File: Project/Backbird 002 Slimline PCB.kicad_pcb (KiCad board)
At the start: 2 copper layers, 14 x 116 mm, 8 parts

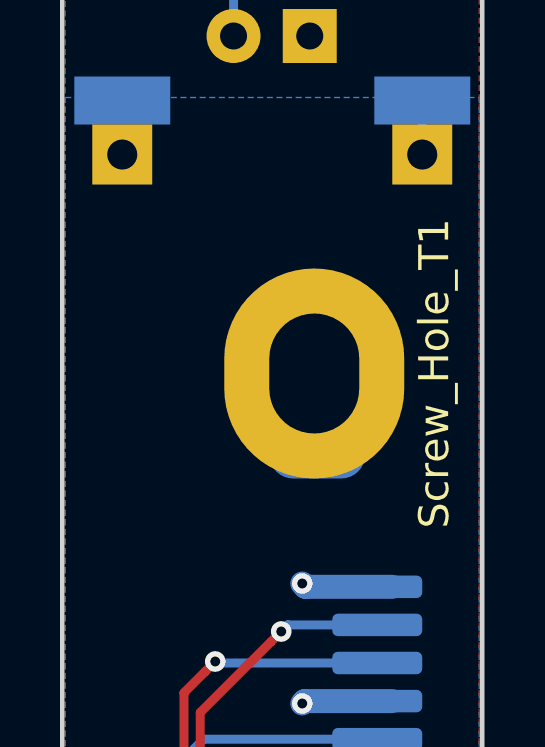
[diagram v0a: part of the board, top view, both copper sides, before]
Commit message: Moved top screw hole closer to edge
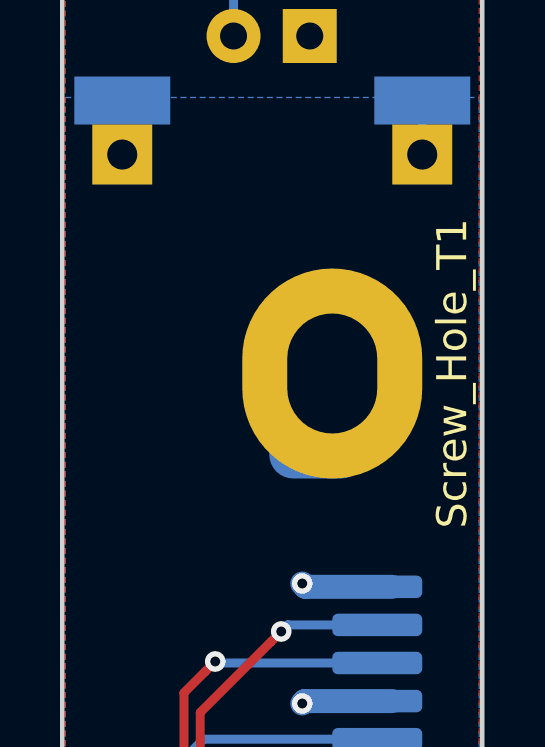
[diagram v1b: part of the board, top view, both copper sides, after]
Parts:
- moved Screw_Hole_T1 0.60 mm to (109.3, 49.5)
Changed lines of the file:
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@@
   )
   (module ProjectFootprints:Blackbird002_Slimline_PCB_Screw_Long (layer F.Cu)
-    (at 108.7 49.48 90)
+    (at 109.3 49.48 90)
     (fp_text reference Screw_Hole_T1 (at 0 4 90) (layer F.SilkS)
       (effects (font (size 1 1) (thickness 0.15)))

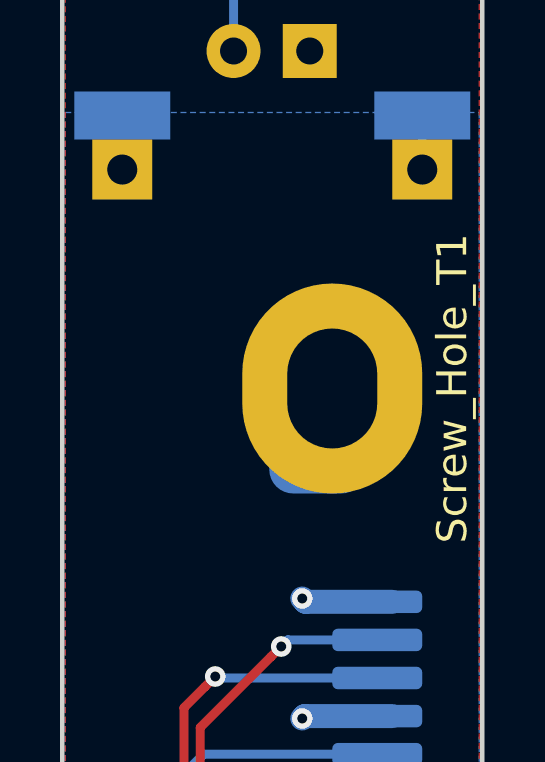
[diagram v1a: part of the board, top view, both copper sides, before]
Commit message: Shrank top (long) screw hole by 0.5mm on each dimension
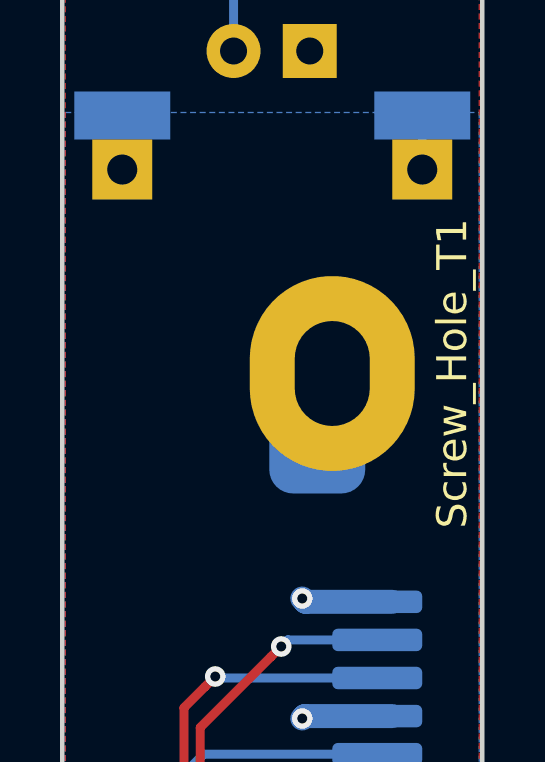
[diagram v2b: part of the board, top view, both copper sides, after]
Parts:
- moved Screw_Hole_T1 0.50 mm to (109.3, 49.0)
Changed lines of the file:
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@@
     (add_net "Net-(Screw_Hole_T1-Pad1)")
+  )
+  (module ProjectFootprints:Blackbird002_Slimline_PCB_Screw_Long (layer F.Cu)
+    (at 109.3 48.98 90)
+    (fp_text reference Screw_Hole_T1 (at 0 4 90) (layer F.SilkS)
+      (effects (font (size 1 1) (thickness 0.15)))
+    )
+    (fp_text value Conn_01x01 (at 0 -3.5 90) (layer F.Fab)
+      (effects (font (size 1 1) (thickness 0.15)))
+    )
+    (pad 1 thru_hole oval (at 0 0 90) (size 6.5 5.5) (drill oval 3.5 2.5) (layers *.Cu *.Mask)
+      (net 11 "Net-(Screw_Hole_T1-Pad1)"))
   )
   (module ProjectFootprints:Blackbird002_Slimline_PCB_Screw (layer F.Cu)
@@
       (net 1 "Net-(D1-Pad2)"))
   )
-  (module ProjectFootprints:Blackbird002_Slimline_PCB_Screw_Long (layer F.Cu)
-    (at 109.3 49.48 90)
-    (fp_text reference Screw_Hole_T1 (at 0 4 90) (layer F.SilkS)
-      (effects (font (size 1 1) (thickness 0.15)))
-    )
-    (fp_text value Conn_01x01 (at 0 -3.5 90) (layer F.Fab)
-      (effects (font (size 1 1) (thickness 0.15)))
-    )
-    (pad 1 thru_hole oval (at 0 0 90) (size 7 6) (drill oval 4 3) (layers *.Cu *.Mask)
-      (net 11 "Net-(Screw_Hole_T1-Pad1)"))
-  )
   (dimension 5 (width 0.3) (layer Eco1.User)

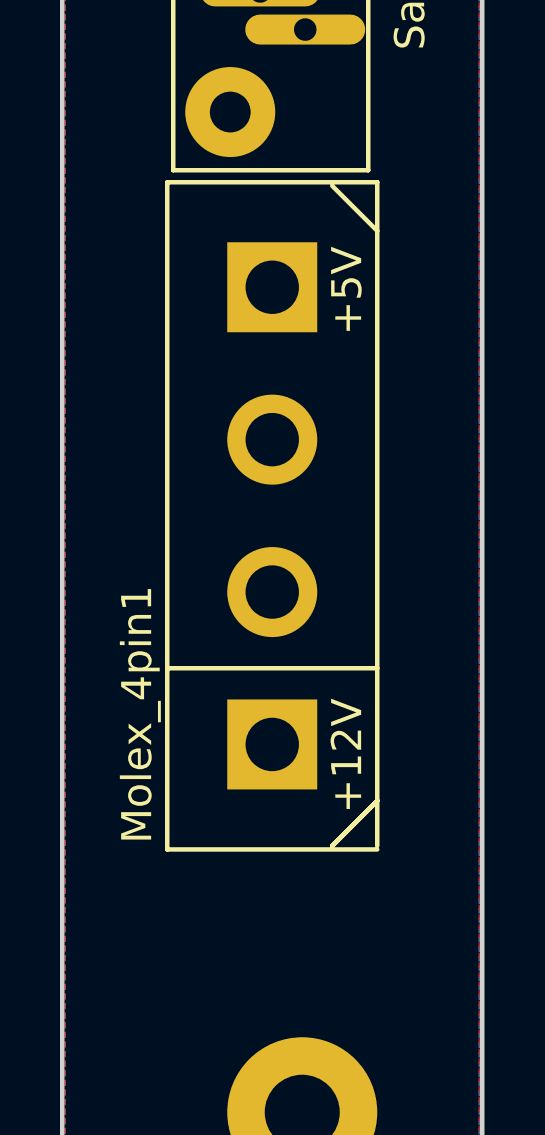
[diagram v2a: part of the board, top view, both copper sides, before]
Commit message: Moved 4pin power connector down ~3mm
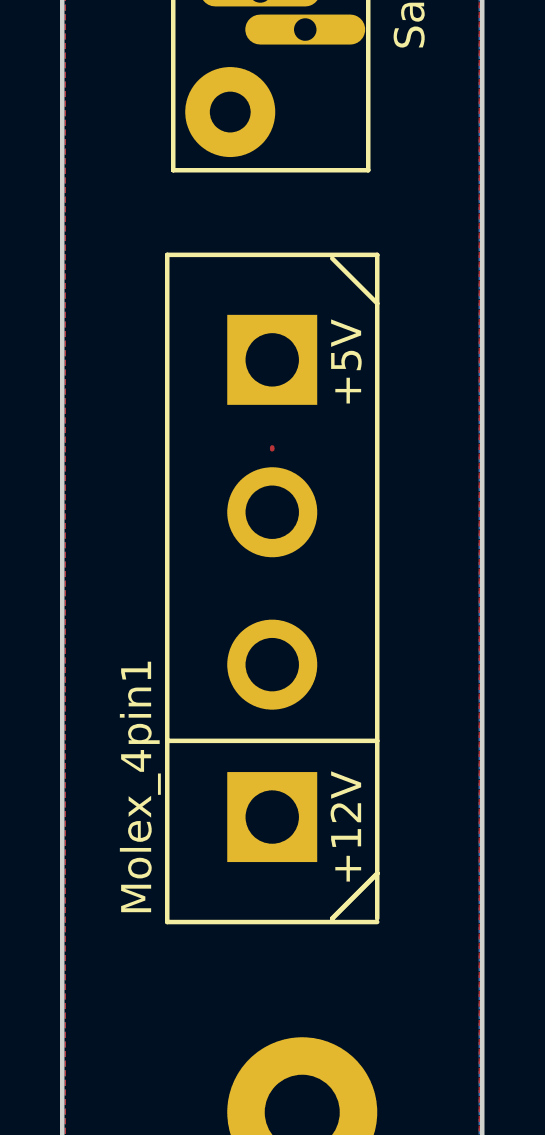
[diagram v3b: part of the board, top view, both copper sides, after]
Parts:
- moved Molex_4pin1 2.42 mm to (107.3, 120.5)
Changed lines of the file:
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@@
   )
   (module ProjectFootprints:MOLEX_8981_0015244745 (layer F.Cu)
-    (at 107.3 118.1 90)
+    (at 107.3 120.52 90)
     (fp_text reference Molex_4pin1 (at -6.62 -4.5 90) (layer F.SilkS)
       (effects (font (size 1 1) (thickness 0.15)))

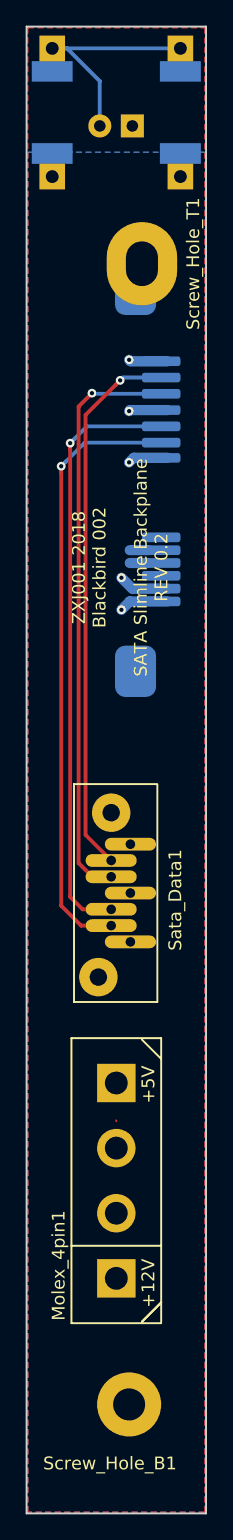
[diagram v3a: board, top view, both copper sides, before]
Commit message: Traces are now at least 0.5mm wide. Added more traces for the +5V SATA power connector
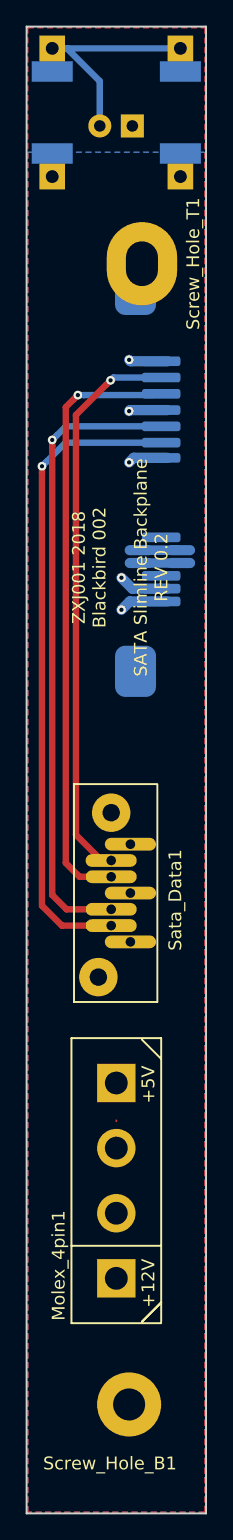
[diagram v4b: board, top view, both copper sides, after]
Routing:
- net +5V: track 2.90 -> 5.80 mm
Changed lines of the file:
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@@
     (thickness 1.6)
     (drawings 26)
-    (tracks 60)
+    (tracks 63)
     (zones 0)
     (modules 8)
@@
   (gr_line (start 114.3 30.48) (end 114.3 146.48) (layer Eco1.User) (width 0.2))
   (gr_line (start 100.3 30.48) (end 114.3 30.48) (layer Eco1.User) (width 0.2))
-  (segment (start 103.45189 32.17914) (end 102.3 32.17914) (width 0.3) (layer B.Cu) (net 1))
-  (segment (start 106.01 38.23) (end 106.01 34.73725) (width 0.3) (layer B.Cu) (net 1))
-  (segment (start 106.01 34.73725) (end 103.45189 32.17914) (width 0.3) (layer B.Cu) (net 1))
-  (segment (start 112.3 32.17914) (end 102.3 32.17914) (width 0.3) (layer B.Cu) (net 1))
+  (segment (start 113.05 71.33) (end 111.6 71.33) (width 0.8) (layer B.Cu) (net 3))
+  (segment (start 113.05 72.33) (end 111.6 72.33) (width 0.8) (layer B.Cu) (net 3))
+  (segment (start 103.45189 32.17914) (end 102.3 32.17914) (width 0.5) (layer B.Cu) (net 1))
+  (segment (start 106.01 34.73725) (end 103.45189 32.17914) (width 0.5) (layer B.Cu) (net 1))
+  (segment (start 106.01 38.23) (end 106.01 34.73725) (width 0.5) (layer B.Cu) (net 1))
+  (segment (start 112.3 32.17914) (end 102.3 32.17914) (width 0.5) (layer B.Cu) (net 1))
   (segment (start 102.3 32.17914) (end 102.3 33.98) (width 0.3) (layer B.Cu) (net 1))
   (segment (start 112.3 32.17914) (end 112.3 33.98) (width 0.3) (layer B.Cu) (net 1))
@@
   (segment (start 109.8 71.33) (end 108.35 71.33) (width 0.8) (layer B.Cu) (net 3))
   (segment (start 109.8 72.33) (end 108.35 72.33) (width 0.8) (layer B.Cu) (net 3))
-  (segment (start 104.84 62.94) (end 103.342899 64.437101) (width 0.3) (layer B.Cu) (net 4) (status 1000000))
-  (segment (start 103 65.264933) (end 103 64.78) (width 0.3) (layer F.Cu) (net 4) (status 1000000))
-  (segment (start 111.3 62.94) (end 104.84 62.94) (width 0.3) (layer B.Cu) (net 4) (status 1000000))
-  (segment (start 103.342899 64.437101) (end 103 64.78) (width 0.3) (layer B.Cu) (net 4) (status 1000000))
-  (segment (start 103 99.064933) (end 103 65.264933) (width 0.3) (layer F.Cu) (net 4) (status 1000000))
-  (segment (start 104.555067 100.62) (end 103 99.064933) (width 0.3) (layer F.Cu) (net 4) (status 1000000))
-  (segment (start 106.9 100.62) (end 104.555067 100.62) (width 0.3) (layer F.Cu) (net 4) (status 1000000))
-  (via (at 103 64.78) (size 0.6858) (drill 0.3302) (layers F.Cu B.Cu) (net 4) (status 1000000))
+  (via (at 101.5 64.78) (size 0.6858) (drill 0.3302) (layers F.Cu B.Cu) (net 4))
+  (segment (start 103.055067 100.62) (end 101.5 99.064933) (width 0.5) (layer F.Cu) (net 4))
+  (segment (start 101.5 99.064933) (end 101.5 65.264933) (width 0.5) (layer F.Cu) (net 4))
+  (segment (start 105.4 100.62) (end 103.055067 100.62) (width 0.5) (layer F.Cu) (net 4))
+  (segment (start 101.5 65.264933) (end 101.5 64.78) (width 0.5) (layer F.Cu) (net 4))
+  (segment (start 109.8 62.94) (end 103.34 62.94) (width 0.5) (layer B.Cu) (net 4))
+  (segment (start 103.34 62.94) (end 101.842899 64.437101) (width 0.5) (layer B.Cu) (net 4))
+  (segment (start 101.842899 64.437101) (end 101.5 64.78) (width 0.5) (layer B.Cu) (net 4))
   (segment (start 106.9 99.35) (end 106.238934 99.35) (width 0.1524) (layer F.Cu) (net 5))
-  (segment (start 103.700002 63.464933) (end 103.700002 62.98) (width 0.3) (layer F.Cu) (net 5))
-  (segment (start 111.3 61.67) (end 105.010002 61.67) (width 0.3) (layer B.Cu) (net 5))
-  (segment (start 105.010002 61.67) (end 104.042901 62.637101) (width 0.3) (layer B.Cu) (net 5))
-  (segment (start 106.9 99.35) (end 104.67 99.35) (width 0.3) (layer F.Cu) (net 5))
-  (segment (start 104.042901 62.637101) (end 103.700002 62.98) (width 0.3) (layer B.Cu) (net 5))
-  (segment (start 104.67 99.35) (end 103.700002 98.380002) (width 0.3) (layer F.Cu) (net 5))
-  (segment (start 103.700002 98.380002) (end 103.700002 63.464933) (width 0.3) (layer F.Cu) (net 5))
-  (via (at 103.700002 62.98) (size 0.6858) (drill 0.3302) (layers F.Cu B.Cu) (net 5))
-  (segment (start 111.3 59.13) (end 105.45 59.13) (width 0.3) (layer B.Cu) (net 6))
-  (segment (start 104.357101 60.122899) (end 105.057101 59.422899) (width 0.3) (layer F.Cu) (net 6))
-  (segment (start 105.45 59.13) (end 105.4 59.08) (width 0.3) (layer B.Cu) (net 6))
-  (segment (start 105.057101 59.422899) (end 105.4 59.08) (width 0.3) (layer F.Cu) (net 6))
-  (segment (start 105.43 96.81) (end 104.357101 95.737101) (width 0.3) (layer F.Cu) (net 6))
-  (segment (start 104.357101 95.737101) (end 104.357101 60.122899) (width 0.3) (layer F.Cu) (net 6))
-  (segment (start 106.9 96.81) (end 105.43 96.81) (width 0.3) (layer F.Cu) (net 6))
-  (via (at 105.4 59.08) (size 0.6858) (drill 0.3302) (layers F.Cu B.Cu) (net 6))
-  (segment (start 106.9 95.54) (end 104.9 93.54) (width 0.3) (layer F.Cu) (net 7))
-  (segment (start 111.3 57.86) (end 107.819992 57.86) (width 0.3) (layer B.Cu) (net 7))
-  (segment (start 104.9 60.779992) (end 107.257093 58.422899) (width 0.3) (layer F.Cu) (net 7))
-  (segment (start 107.257093 58.422899) (end 107.599992 58.08) (width 0.3) (layer F.Cu) (net 7))
-  (segment (start 104.9 93.54) (end 104.9 60.779992) (width 0.3) (layer F.Cu) (net 7))
-  (segment (start 107.819992 57.86) (end 107.599992 58.08) (width 0.3) (layer B.Cu) (net 7))
-  (via (at 107.599992 58.08) (size 0.6858) (drill 0.3302) (layers F.Cu B.Cu) (net 7))
+  (segment (start 103.36 61.67) (end 102.642899 62.387101) (width 0.5) (layer B.Cu) (net 5))
+  (segment (start 110.05 61.67) (end 103.36 61.67) (width 0.5) (layer B.Cu) (net 5))
+  (segment (start 102.642899 62.387101) (end 102.3 62.73) (width 0.5) (layer B.Cu) (net 5))
+  (segment (start 102.3 98.23) (end 102.3 63.214933) (width 0.5) (layer F.Cu) (net 5))
+  (segment (start 102.3 63.214933) (end 102.3 62.73) (width 0.5) (layer F.Cu) (net 5))
+  (segment (start 103.42 99.35) (end 102.3 98.23) (width 0.5) (layer F.Cu) (net 5))
+  (segment (start 105.65 99.35) (end 103.42 99.35) (width 0.5) (layer F.Cu) (net 5))
+  (via (at 102.3 62.73) (size 0.6858) (drill 0.3302) (layers F.Cu B.Cu) (net 5))
+  (via (at 104.3 59.230006) (size 0.6858) (drill 0.3302) (layers F.Cu B.Cu) (net 6))
+  (segment (start 103.357101 95.737101) (end 103.357101 60.172905) (width 0.5) (layer F.Cu) (net 6))
+  (segment (start 103.957101 59.572905) (end 104.3 59.230006) (width 0.5) (layer F.Cu) (net 6))
+  (segment (start 105.9 96.81) (end 104.43 96.81) (width 0.5) (layer F.Cu) (net 6))
+  (segment (start 104.43 96.81) (end 103.357101 95.737101) (width 0.5) (layer F.Cu) (net 6))
+  (segment (start 110.3 59.13) (end 110.199994 59.230006) (width 0.5) (layer B.Cu) (net 6))
+  (segment (start 103.357101 60.172905) (end 103.957101 59.572905) (width 0.5) (layer F.Cu) (net 6))
+  (segment (start 110.199994 59.230006) (end 104.784933 59.230006) (width 0.5) (layer B.Cu) (net 6))
+  (segment (start 104.784933 59.230006) (end 104.3 59.230006) (width 0.5) (layer B.Cu) (net 6))
+  (segment (start 106.15 95.54) (end 104.15 93.54) (width 0.5) (layer F.Cu) (net 7))
+  (via (at 106.849992 58.08) (size 0.6858) (drill 0.3302) (layers F.Cu B.Cu) (net 7))
+  (segment (start 107.069992 57.86) (end 106.849992 58.08) (width 0.5) (layer B.Cu) (net 7))
+  (segment (start 104.15 93.54) (end 104.15 60.779992) (width 0.5) (layer F.Cu) (net 7))
+  (segment (start 106.507093 58.422899) (end 106.849992 58.08) (width 0.5) (layer F.Cu) (net 7))
+  (segment (start 104.15 60.779992) (end 106.507093 58.422899) (width 0.5) (layer F.Cu) (net 7))
+  (segment (start 110.55 57.86) (end 107.069992 57.86) (width 0.5) (layer B.Cu) (net 7))
   (zone (net 3) (net_name +5V) (layer B.Cu) (hatch edge 0.508)
     (connect_pads (clearance 0.508))
